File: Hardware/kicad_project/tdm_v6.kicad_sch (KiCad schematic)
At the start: 39 parts, among them J1 picoprobe_debug, J2 USB_C_Receptacle_USB2.0, SW26 spst_4_pin_internal, SW27 spst_4_pin_internal, U1 W25Q32JVSS, U2 RP2040, Y1 Crystal_GND24

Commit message: v9 hardware
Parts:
- D2: LCSC c2286 -> C2286
- SW26, SW27: footprint RandomJunk:ts1102_smallerpads_buttonhole -> MyLibrary:SKSCLDE010; LCSC C480275 -> C115362
- Y1: LCSC C97242 -> C5332006

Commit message: v10 board
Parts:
- added C66: 2u2, Capacitor_SMD:C_0402_1005Metric, symbol Device:C
- C1, C2, C26, C27, C28, C29, C3, C30, C31, C32, C33, C34, C35, C36, C37: footprint Capacitors_SMD:C_0402_NoSilk -> Capacitor_SMD:C_0402_1005Metric; checked (none) -> 1
- D2, J2, RV1, RV2, SW26, SW27, U1, U2: checked (none) -> 1
- R1, R19, R2, R20, R3, R31, R4, R5, R6, R7: footprint Resistors_SMD:R_0402_NoSilk -> Resistor_SMD:R_0402_1005Metric; checked (none) -> 1
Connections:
- net +3V3: no longer RV1.1, RV2.1, U2.43 (ADC_AVDD)
- net GND: now also C66.2
- net amp_control: no longer U2.41 (GPIO29_ADC3)
- new net usb_sense: U2.41 (GPIO29_ADC3)
- new net vref2.5: C66.1, RV1.1, RV2.1, U2.43 (ADC_AVDD)
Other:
- sheet Power ports: added usb_sense; removed none
- moved on the sheet: C1, C2, C26, C27, C28, C29, C3, C30, C31, C32, C33, C34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

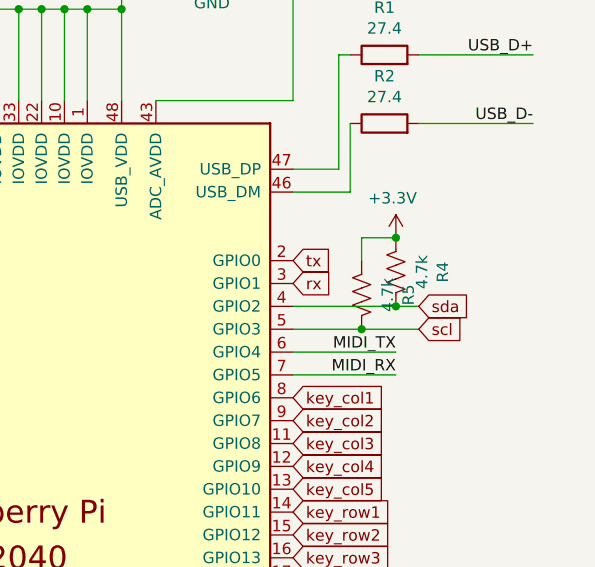
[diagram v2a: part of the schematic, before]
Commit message: corrected the i2c pullups
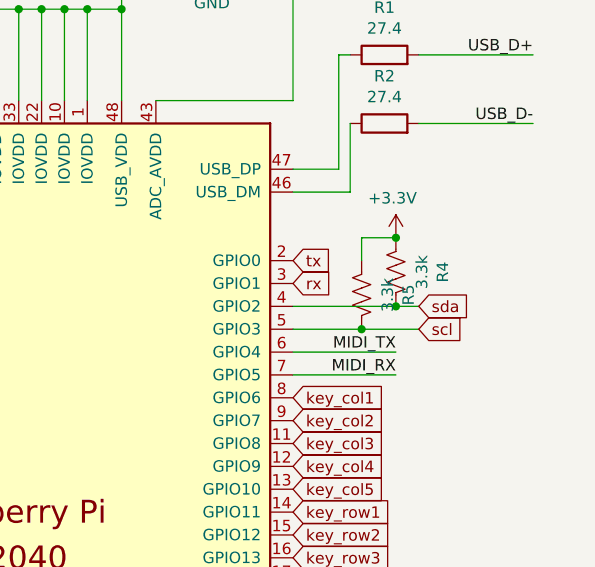
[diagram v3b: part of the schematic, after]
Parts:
- R4, R5: value 4.7k -> 3.3k; footprint Resistor_SMD:R_0402_1005Metric -> MyLibrary:R_0402_1005Metric_nosilk; LCSC C25900 -> C25890
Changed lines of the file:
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@@
     (in_bom yes) (on_board yes)
     (property "Reference" "R4" (id 0) (at 268.097 74.93 90))
-    (property "Value" "4.7k" (id 1) (at 265.7856 74.93 90))
-    (property "Footprint" "Resistor_SMD:R_0402_1005Metric" (id 2) (at 261.874 75.184 90)
+    (property "Value" "3.3k" (id 1) (at 265.7856 74.93 90))
+    (property "Footprint" "MyLibrary:R_0402_1005Metric_nosilk" (id 2) (at 261.874 75.184 90)
       (effects (font (size 1.27 1.27)) hide)
     )
@@
       (effects (font (size 1.27 1.27)) hide)
     )
-    (property "LCSC" "C25900" (id 4) (at 262.89 74.93 0)
+    (property "LCSC" "C25890" (id 4) (at 262.89 74.93 0)
       (effects (font (size 1.27 1.27)) hide)
     )
@@
     (in_bom yes) (on_board yes)
     (property "Reference" "R5" (id 0) (at 264.287 77.47 90))
-    (property "Value" "4.7k" (id 1) (at 261.9756 77.47 90))
-    (property "Footprint" "Resistor_SMD:R_0402_1005Metric" (id 2) (at 258.064 77.724 90)
+    (property "Value" "3.3k" (id 1) (at 261.9756 77.47 90))
+    (property "Footprint" "MyLibrary:R_0402_1005Metric_nosilk" (id 2) (at 258.064 77.724 90)
       (effects (font (size 1.27 1.27)) hide)
     )
@@
       (effects (font (size 1.27 1.27)) hide)
     )
-    (property "LCSC" "C25900" (id 4) (at 259.08 77.47 0)
+    (property "LCSC" "C25890" (id 4) (at 259.08 77.47 0)
       (effects (font (size 1.27 1.27)) hide)
     )
@@
     )
     (path "/00000000-0000-0000-0000-0000608aeeb4"
-      (reference "R4") (unit 1) (value "4.7k") (footprint "Resistor_SMD:R_0402_1005Metric")
+      (reference "R4") (unit 1) (value "3.3k") (footprint "MyLibrary:R_0402_1005Metric_nosilk")
     )
     (path "/00000000-0000-0000-0000-0000608aeeba"
-      (reference "R5") (unit 1) (value "4.7k") (footprint "Resistor_SMD:R_0402_1005Metric")
+      (reference "R5") (unit 1) (value "3.3k") (footprint "MyLibrary:R_0402_1005Metric_nosilk")
     )
     (path "/00000000-0000-0000-0000-000061f9f041"

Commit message: v11 hardware
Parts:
- D2: value LED -> LEDGreen; LCSC C2286 -> C72043
- RV1, RV2: LCSC C209779 -> (none)
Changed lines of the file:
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@@
       (effects (font (size 1.27 1.27)) hide)
     )
-    (property "LCSC" "C209779" (id 4) (at 52.07 39.37 0)
+    (property "LCSC" "" (id 4) (at 52.07 39.37 0)
       (effects (font (size 1.27 1.27)) hide)
     )
@@
       (effects (font (size 1.27 1.27)) hide)
     )
-    (property "LCSC" "C209779" (id 4) (at 74.93 39.37 0)
+    (property "LCSC" "" (id 4) (at 74.93 39.37 0)
       (effects (font (size 1.27 1.27)) hide)
     )
@@
     (in_bom yes) (on_board yes)
     (property "Reference" "D2" (id 0) (at 269.4178 142.6464 0))
-    (property "Value" "LED" (id 1) (at 269.4178 140.335 0))
+    (property "Value" "LEDGreen" (id 1) (at 269.4178 140.335 0))
     (property "Footprint" "LEDs:LED_0603" (id 2) (at 269.24 137.16 0)
       (effects (font (size 1.27 1.27)) hide)
@@
       (effects (font (size 1.27 1.27)) hide)
     )
-    (property "LCSC" "C2286" (id 4) (at 269.24 137.16 0)
+    (property "LCSC" "C72043" (id 4) (at 269.24 137.16 0)
       (effects (font (size 1.27 1.27)) hide)
     )
@@
     )
     (path "/00000000-0000-0000-0000-00006262bf3c"
-      (reference "D2") (unit 1) (value "LED") (footprint "LEDs:LED_0603")
+      (reference "D2") (unit 1) (value "LEDGreen") (footprint "LEDs:LED_0603")
     )
     (path "/00000000-0000-0000-0000-000062e6c628/ac2edd9a-51e8-4c53-9f80-120ab8424046"
@@
     )
     (path "/00000000-0000-0000-0000-00006366865e/1f752e1b-fae3-477e-9a34-c4ecad4a9981"
-      (reference "R23") (unit 1) (value "5k") (footprint "Resistor_SMD:R_0402_1005Metric")
+      (reference "R23") (unit 1) (value "5.1k") (footprint "Resistor_SMD:R_0402_1005Metric")
     )
     (path "/00000000-0000-0000-0000-000062e6c628/00000000-0000-0000-0000-000061d6fe54"
